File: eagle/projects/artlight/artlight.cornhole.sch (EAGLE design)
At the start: 21 parts, among them T1 2N2222, T2 2N2222, T3 2N2222, T4 2N2222, T5 2N2222, T6 2N2222

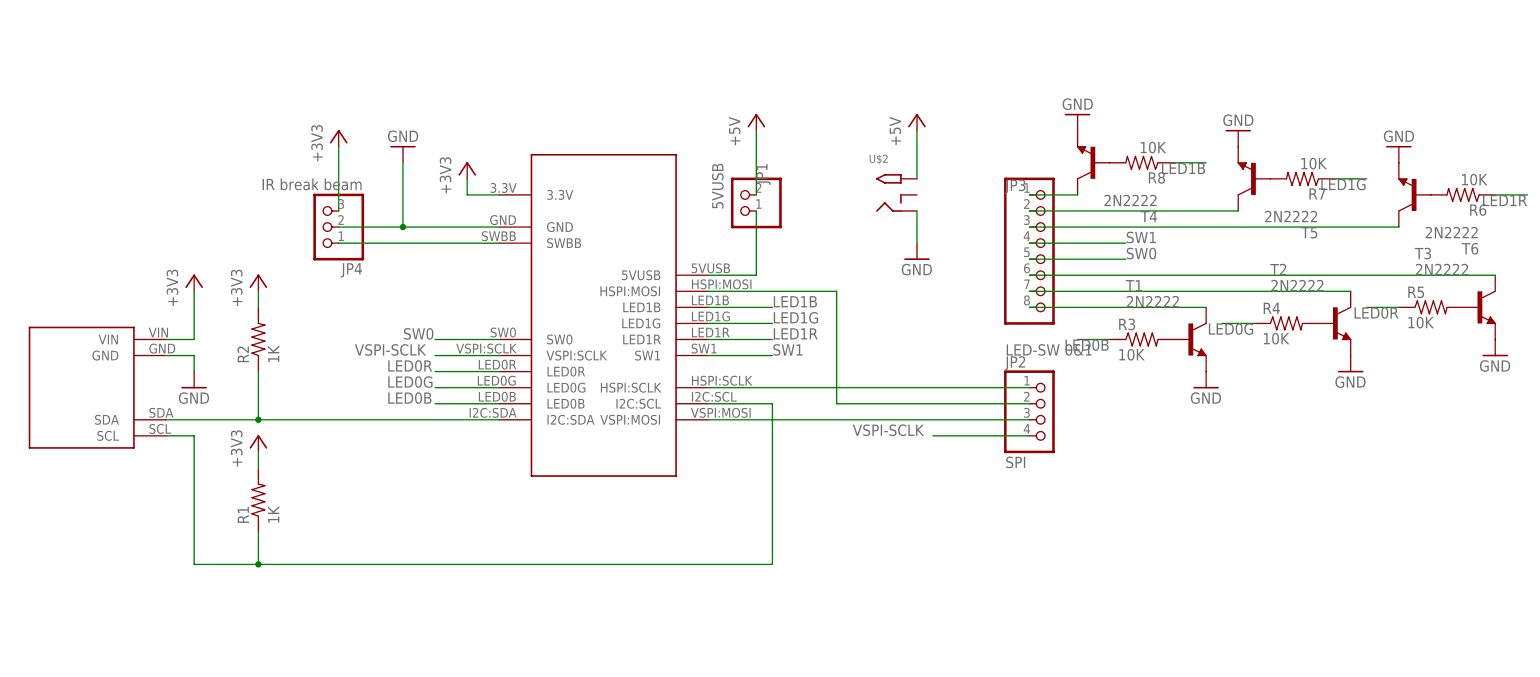
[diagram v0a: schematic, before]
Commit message: eagle: artlight.cornhole: fix ground pour, add ledsw2
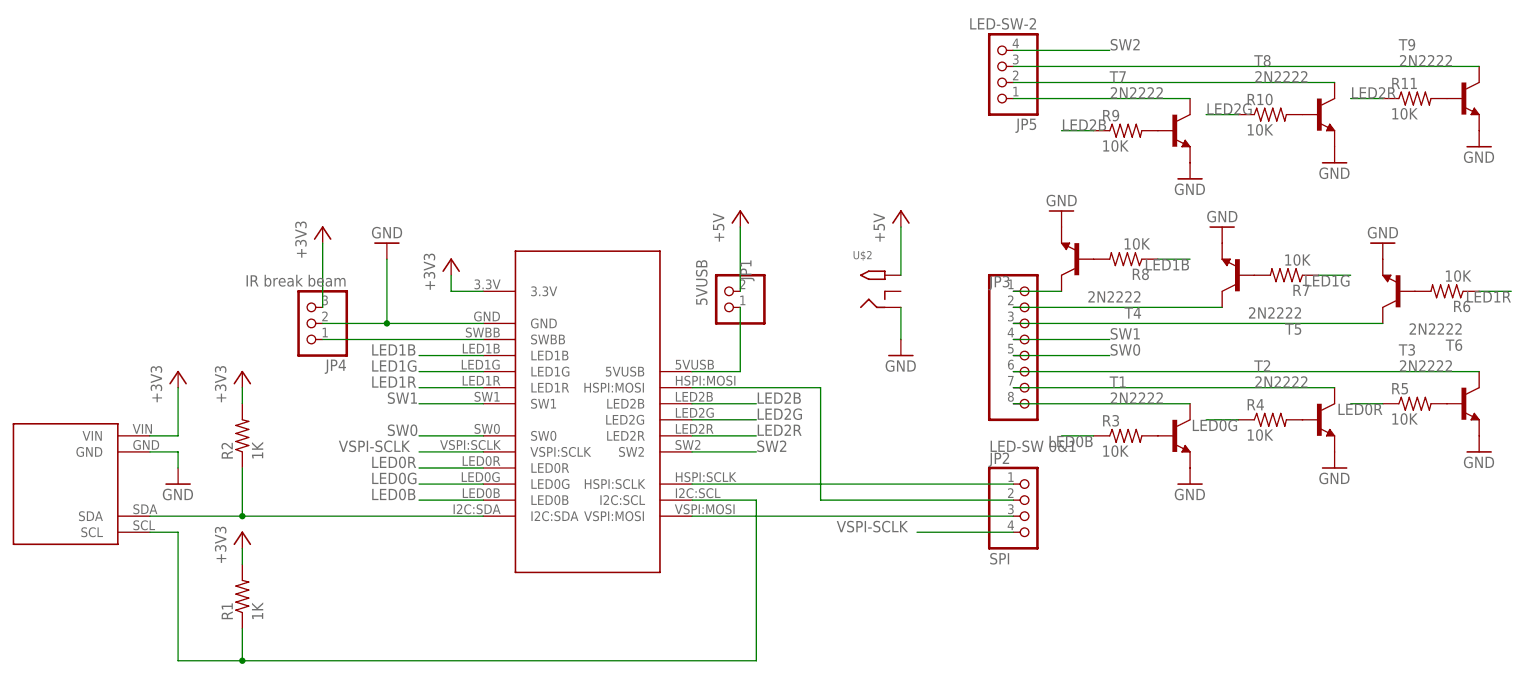
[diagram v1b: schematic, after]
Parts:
- added JP5: LED-SW-2, pinhead:PINHD-1X4
- added R10, R11, R9: 10K, rcl:R-US_0204/2V
- added T7, T8, T9: 2N2222, adafruit:2N2222
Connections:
- new net LED2B: R9.1, U$1.LED2B
- new net LED2B-BASE: R9.2, T7.B
- new net LED2B-PIN: JP5.1, T7.C
- new net LED2G: R10.1, U$1.LED2G
- new net LED2G-BASE: R10.2, T8.B
- new net LED2G-PIN: JP5.2, T8.C
- new net LED2R: R11.1, U$1.LED2R
- new net LED2R-BASE: R11.2, T9.B
- new net LED2R-PIN: JP5.3, T9.C
- new net SW2: JP5.4, U$1.SW2
- net GND: now also T7.E, T8.E, T9.E
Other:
- moved on the sheet: JP1, JP2, JP3, JP4, R1, R2, R3, R4, R5, R6, R7, R8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

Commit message: eagle: artlight.cornhole, pins
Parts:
- added R12, R13: 47K, rcl:R-US_0204/7
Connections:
- net +3V3: now also R12.2, R13.2
- net SW1: now also R12.1
- net SWBB: now also R13.1
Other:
- moved on the sheet: JP4, R1, R2
